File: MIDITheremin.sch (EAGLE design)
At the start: 47 parts, among them IC1 TL072P, T1 2N3904, T2 2N3904, T3 2N3904, T4 2N3904

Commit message: Add files via upload
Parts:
- added C14: 22pF, resistor:C-EU050-025X075
- added C15, C20: 1uF, resistor:CPOL-USE2.5-7
- added IC2: TL072P, linear:TL072P
- added R18, R24, R25, R26: 10k, resistor:R-US_0411/3V
- added R20: 470, resistor:R-US_0411/3V
- added R23: 33, resistor:R-US_0411/3V
- added R27, R28, R30: 100k, resistor:R-US_0411/3V
- added R29: 10k, pot:TRIM_US-B64Y
- added T5: 2N3904, transistor-neu-to92:2N3904
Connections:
- removed net N$20: C10.A, C3.1, C4.2, C5.1, L2.2, T3.C
- new net LOCAL_RESONANCE: C10.A, C14.1, C3.1, C4.2, C5.1, L2.2, T3.C, T5.C
- new net N$21: R20.1, T5.B
- new net N$22: C14.2, R20.2, R23.1
- new net N$23: C15.+, R23.2, R24.2, R25.2
- new net N$24: IC2A.OUT, R26.2, R27.1
- new net N$25: IC2A.-IN, R27.2, R28.1, R30.1
- new net N$26: R28.2, R29.S
- new net N$9: C15.-, C20.-, R18.2, R26.1, T5.E
- new net V_CONTROL: R30.2
- net GND: now also C20.+, IC2A.+IN, R25.1, R29.E
- net L_OSC_V-: now also R18.1, R24.1
- net V+: now also IC2P.V+
- net V-: now also IC2P.V-, R29.A
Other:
- note added: "Tune this trim to the mid-point of the voltage control"
- moved on the sheet: C10, C3, C4, C5, IC1B, L2, R12, R13, R14, R5, R6, R7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

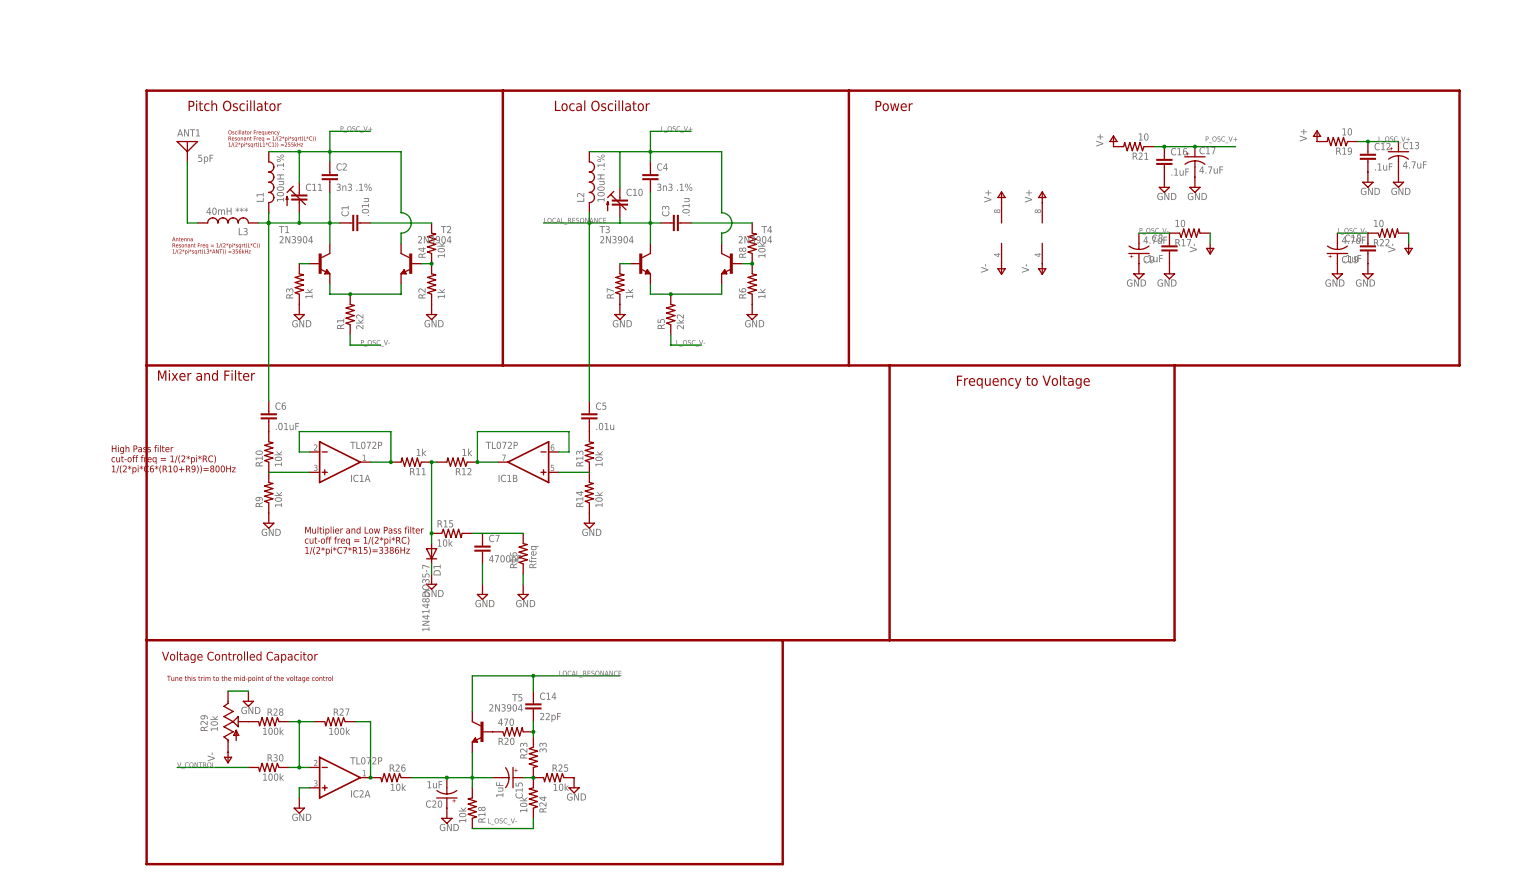
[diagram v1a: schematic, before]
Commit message: renamed theremin boards
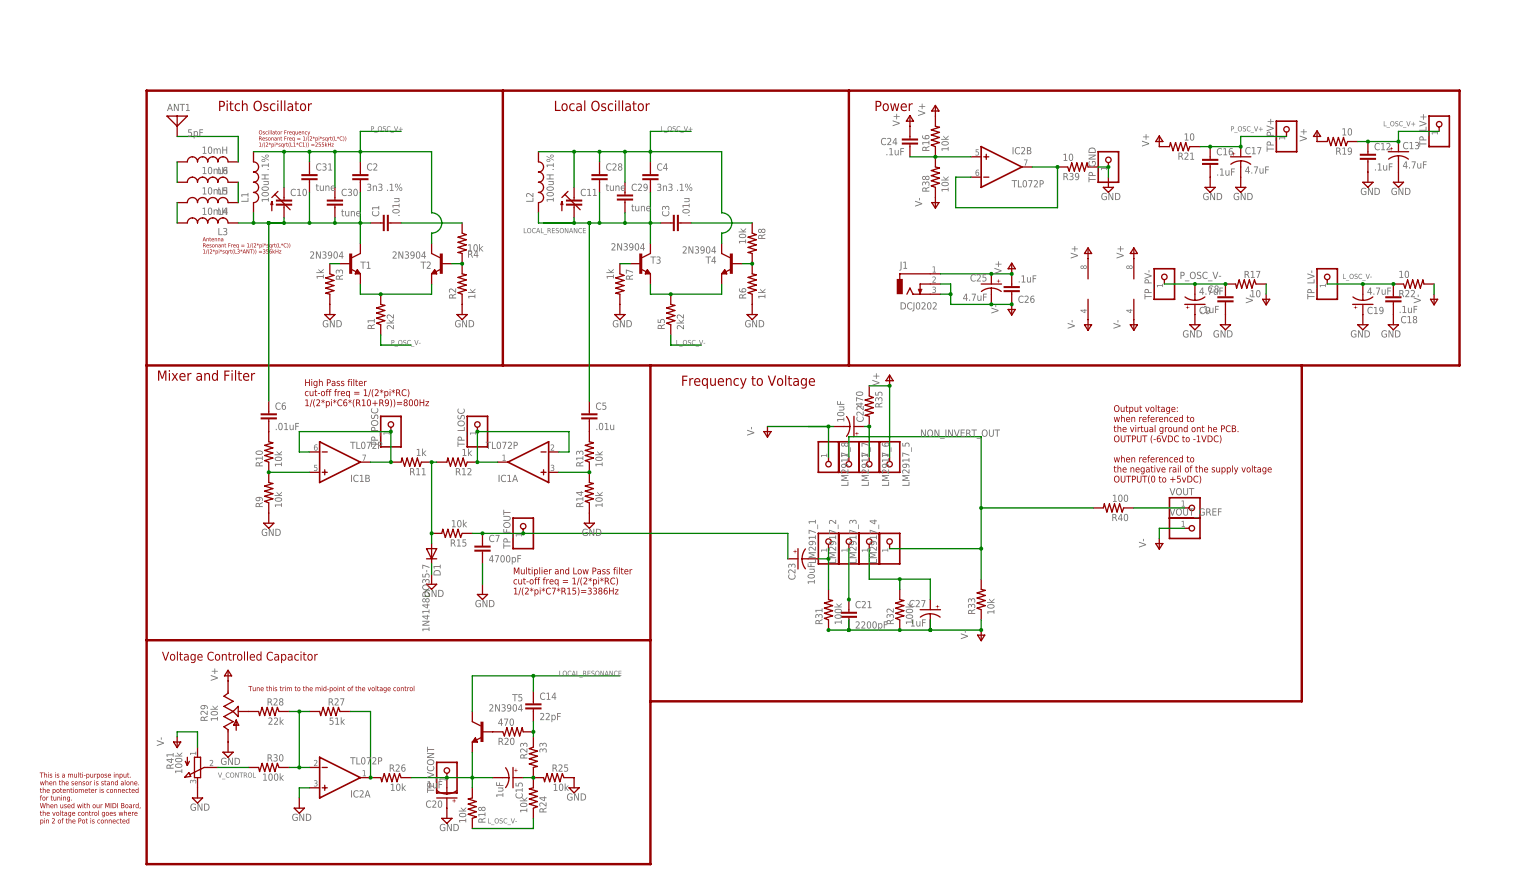
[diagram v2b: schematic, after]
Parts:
- added C21: 2200pF, resistor:C-EU050-025X075
- added C22, C23: 10uF, resistor:CPOL-USE2.5-7
- added C24, C26: .1uF, resistor:C-EU050-025X075
- added C25: 4.7uF, resistor:CPOL-USE2.5-7
- added C27: 1uF, resistor:CPOL-USE2.5-7
- added C28, C29, C30, C31: tune, resistor:C-EU050-025X075
- added J1: DCJ0202, con-jack:DCJ0202
- added L4, L5, L6: 10mH, rcl:L-US6000-XXX-RC
- added LM2917_1, LM2917_2, LM2917_3, LM2917_4, LM2917_5, LM2917_6, LM2917_7, LM2917_8, TP_FOUT, TP_GND, TP_LOSC, TP_LV+, TP_LV-, TP_POSC, TP_PV+, TP_PV-, TP_VCONT, VOUT, VOUT_GREF: (no value), pinhead:PINHD-1X1
- added R31, R32: 100k, rcl:R-US_0411/3V
- added R33: 10k, rcl:R-US_0411/3V
- added R35: 470, rcl:R-US_0411/3V
- added R38: 10k, resistor:R-US_0411/3V
- added R39: 10, resistor:R-US_0411/3V
- added R40: 100, rcl:R-US_0411/3V
- added R41: 100k, pot:3RP/1610N
- C10, C11: device c-trimm:C-TRIMM3008 -> rcl:C-TRIMM3040.427
- L1, L2: device resistor:L-US0207/2V -> rcl:L-US6000-XXX-RC
- L3: value 40mH *** -> 10mH; device resistor:L-US0207/2V -> rcl:L-US6000-XXX-RC
- R16: value Rfreq -> 10k
- R27: value 100k -> 51k
- R28: value 100k -> 22k
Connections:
- new net ANT: ANT1.1, L6.2
- new net N$20: C21.1, LM2917_2.1
- new net N$27: IC2B.-IN, IC2B.OUT, R39.1
- new net N$28: L3.1, L4.1
- new net N$31: C22.+, LM2917_6.1, R35.2
- new net N$33: C27.+, LM2917_3.1, R32.2
- new net N$34: C23.-, LM2917_1.1, R31.2
- new net N$35: L4.2, L5.2
- new net N$36: C24.2, IC2B.+IN, R16.1, R38.2
- new net N$38: R40.1, VOUT.1
- new net NON_INVERT_OUT: LM2917_4.1, LM2917_7.1, R33.2, R40.2
- net GND: now also R29.A, R3.2, R39.2, R41.E, R7.2, TP_GND.1; no longer R16.1, R29.E, R3.1, R7.1
- net LOCAL_RESONANCE: now also C11.A, C28.2, C29.2; no longer C10.A
- net L_OSC_V+: now also C11.E, C28.1, C29.1, TP_LV+.1; no longer C10.E
- net L_OSC_V-: now also TP_LV-.1
- net N$11: now also IC1B.-IN, IC1B.OUT, TP_POSC.1; no longer IC1A.-IN, IC1A.OUT
- net N$12: now also IC1A.-IN, IC1A.OUT, TP_LOSC.1; no longer IC1B.-IN, IC1B.OUT
- net N$13: now also IC1B.+IN; no longer IC1A.+IN
- net N$14: now also R15.2; no longer R15.1
- net N$15: now also IC1A.+IN; no longer IC1B.+IN
- net N$16: now also R8.1; no longer R8.2
- net N$18: now also C23.+, R15.1, TP_FOUT.1; no longer R15.2, R16.2
- net N$19: now also L5.1, L6.1; no longer ANT1.1, L3.1
- net N$2: now also R4.2; no longer R4.1
- net N$3: now also R3.1; no longer R3.2
- net N$4: now also C10.A, C30.2, C31.2; no longer C11.A
- net N$5: now also R4.1; no longer R4.2
- net N$7: now also R8.2; no longer R8.1
- net N$8: now also R7.1; no longer R7.2
- net N$9: now also TP_VCONT.1
- net P_OSC_V+: now also C10.E, C30.1, C31.1, TP_PV+.1; no longer C11.E
- net P_OSC_V-: now also R17.2, TP_PV-.1; no longer R17.1
- net V+: now also C24.1, C25.+, C26.2, J1.1, LM2917_5.1, R16.2, R29.E, R35.1
- net V-: now also C21.2, C22.-, C25.-, C26.1, C27.-, J1.2, J1.3, LM2917_8.1, R17.1, R31.1, R32.1, R33.1, R38.1, R41.A, VOUT_GREF.1; no longer R17.2, R29.A
- net V_CONTROL: now also R41.S
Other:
- note added: "Output voltage: when referenced to the virtual ground ont he PCB. OUTPUT (-6VDC to -1VDC) when referenced to the negative rail of the supply voltage OUTPUT(0 to +5vDC)"
- note added: "This is a multi-purpose input. when the sensor is stand alone. the potentiometer is connected for tuning. When used with our MIDI Board, the voltage control goes where pin 2 of the Pot is connected"
- moved on the sheet: ANT1, C1, C10, C11, C16, C17, C18, C19, C2, C8, C9, IC1A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

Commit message: Add files via upload
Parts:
- removed J1: DCJ0202, con-jack:DCJ0202
- removed R41: 100k, pot:3RP/1610N
- removed VOUT_GREF: (no value), pinhead:PINHD-1X1
- added U$1: MIDIJACK, adafruit:MIDIJACK
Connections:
- removed net N$38: R40.1, VOUT.1
- new net VOUT: R40.1, U$1G$1.1, VOUT.1
- net GND: now also U$1G$2.MT, U$1G$3.MT, U$1G$4.MT, U$1G$5.MT; no longer R41.E
- net V+: now also U$1G$1.3; no longer J1.1
- net V-: now also U$1G$1.2; no longer J1.2, J1.3, R41.A, VOUT_GREF.1
- net V_CONTROL: now also U$1G$1.5; no longer R41.S
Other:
- moved on the sheet: C12, C13, C16, C17, C18, C19, C25, C26, C8, C9, R17, R19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
